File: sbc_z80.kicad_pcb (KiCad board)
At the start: 4 copper layers, 101.6 x 50.8 mm, 69 parts, among them J1 RC80 Bus, J2 UPDI TTL, J3 PIO Header, J4 Conn_01x06, J5 Conn_01x06, J6 CTC Header, J7 AVR-JTAG-10, SW1 SW_Push, SW3 SW_DIP_x08, U1 CPU - Z84C0010AEG, U10 74HC04, U11 ATtiny1614-SS, U12 MIC811LUY, U2 TPS7A0533PDBVR, U3 SRAM - IS62C5128BL-45TLI, U4 GLS29EE010, U5 Si5351A-B-GT, U6 SIO/3 - Z84C4310AEG, U7 CPLD - EPM7032STC44, U8 CTC - Z84C3010AEG, U9 PIO - Z84C2010AEG, Y1 25MHZ 8PF

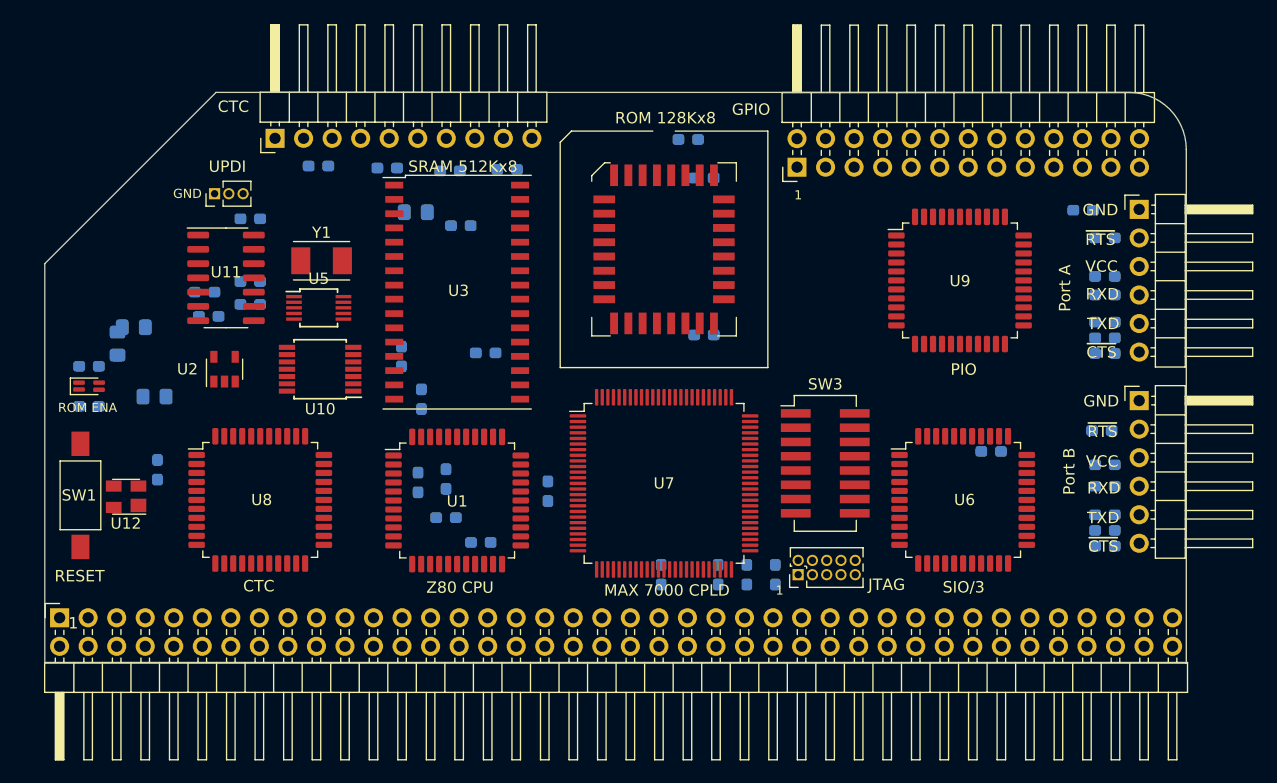
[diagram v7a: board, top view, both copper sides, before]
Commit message: added display, config switch
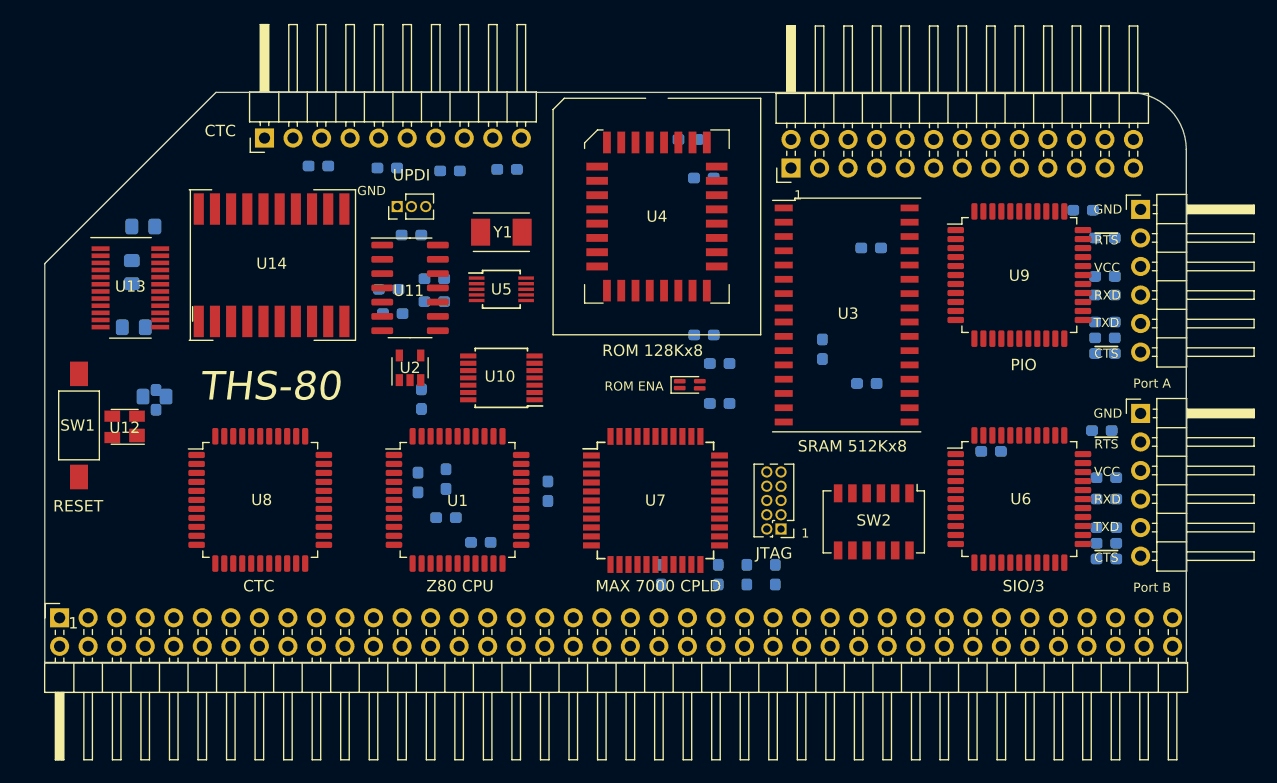
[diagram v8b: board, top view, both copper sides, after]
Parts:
- removed SW3: SW_DIP_x08, Button_Switch_SMD:SW_DIP_SPSTx08_Slide_KingTek_DSHP08TJ_W5.25mm_P1.27mm_JPin
- added G***: LOGO, Logos:asian_tiger, F.Cu at (128.1, 100.2)
- added SW2: SW_DIP_x06, Button_Switch_SMD:SW_DIP_SPSTx06_Slide_Copal_CHS-06A_W5.08mm_P1.27mm_JPin, F.Cu at (149.2, 114.9)
- added U13: AS1115-BSST, Package_SO:QSOP-24_3.9x8.7mm_P0.635mm, F.Cu at (83.1, 94.1)
- added U14: ACDA02-41SGWA-F01, Display:ACDA02-41SGWA-F01, F.Cu at (95.0, 92.1)
- U7: footprint Package_QFP:TQFP-100_14x14mm_P0.5mm -> Package_QFP:TQFP-44_10x10mm_P0.8mm
- moved R29 56.1 mm to (135.5, 100.8)
- moved R30 56.1 mm to (135.5, 104.4)
- moved D1 53.5 mm to (132.8, 102.7)
- moved R21 37.5 mm to (144.7, 99.6)
- moved C14 36.6 mm to (149.0, 90.6)
- moved U3 34.7 mm to (146.8, 96.5)
- moved C5 34.0 mm to (148.6, 102.6)
- moved C2 24.3 mm to (84.2, 88.6)
- moved U2 16.5 mm to (108.0, 101.2)
- moved U11 16.4 mm to (108.0, 94.1)
- moved C16 16.4 mm to (106.4, 96.4)
- moved C15 16.4 mm to (106.0, 94.2)
- moved R1 16.4 mm to (110.1, 93.3)
- moved R2 16.4 mm to (110.1, 95.3)
- moved U5 16.3 mm to (116.1, 94.2)
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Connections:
- net /Clocks/RX renamed /Display and Clocks/RX
- net /Clocks/TX renamed /Display and Clocks/TX
- net Net-(R1-Pad2) renamed /Display and Clocks/SCL
- net Net-(R2-Pad2) renamed /Display and Clocks/SDA
- J1 pad 60: /~PAGE -> (no net)
- U10 pad 11: /PAGE -> /~ROM
- U11 pad 11: (no net) -> /D0
- U11 pad 12: (no net) -> /D1
- U11 pad 13: (no net) -> /D2
- U11 pad 2: (no net) -> /D3
- U11 pad 3: (no net) -> /D4
- U11 pad 4: (no net) -> /D5
- U11 pad 5: (no net) -> /D6
- U11 pad 7: (no net) -> /D7
- U3 pad 22: /~PAGE -> /~RAM
- U3 pad 24: /~MEMRD -> /~RD
- U3 pad 29: /~MEMWR -> /~WR
- U4 pad 22: /PAGE -> /~ROM
- U6 pad 22: (no net) -> /~SIO
- U7 pad 13: /~MREQ -> /~WR
- U7 pad 14: /~RD -> /~MREQ
- U7 pad 15: /~WR -> /~RESET
- U7 pad 18: /~PAGE -> (no net)
- U7 pad 19: /PAGE -> (no net)
- U7 pad 2: /A3 -> /A5
- U7 pad 20: /A18 -> (no net)
- U7 pad 21: /A17 -> (no net)
- U7 pad 22: /A16 -> (no net)
- U7 pad 23: /D3 -> (no net)
- U7 pad 25: /D2 -> (no net)
- U7 pad 27: /D1 -> (no net)
- U7 pad 28: /D0 -> (no net)
- U7 pad 3: /A4 -> /A6
- U7 pad 30: /CTC_CE -> /~PIO
- U7 pad 31: /~MEMRD -> /TDO
- U7 pad 32: /TDO -> /~CTC
- U7 pad 33: /~MEMWR -> /~SIO
- U7 pad 34: (no net) -> /~RAM
- U7 pad 35: (no net) -> /~ROM
- U7 pad 42: /A0 -> /A2
- U7 pad 43: /A1 -> /A3
- U7 pad 44: /A2 -> /A4
- U7 pad 5: /A5 -> /A7
- U7 pad 6: /A6 -> /A15
- U7 pad 8: /A7 -> /A16
- U8 pad 31: /CTC_CE -> /~CTC
- U9 pad 10: (no net) -> /~PIO
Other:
- board text added: "THS-80"
- board text removed: "GPIO"
